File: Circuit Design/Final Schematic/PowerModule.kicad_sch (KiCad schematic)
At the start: 11 parts

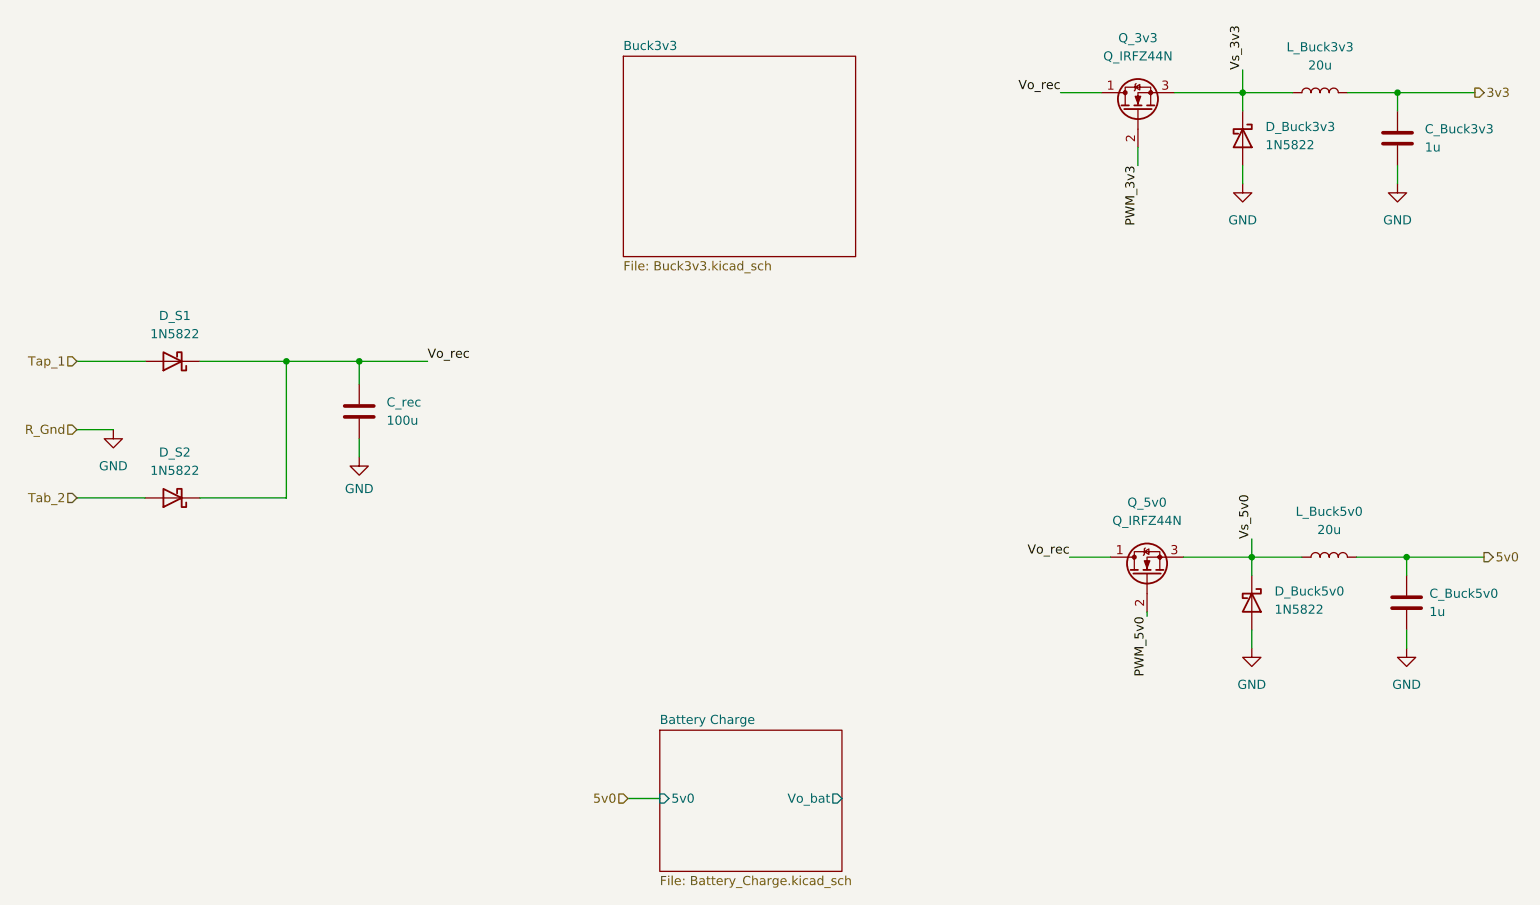
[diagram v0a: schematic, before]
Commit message: Power Module on schematic almost ready
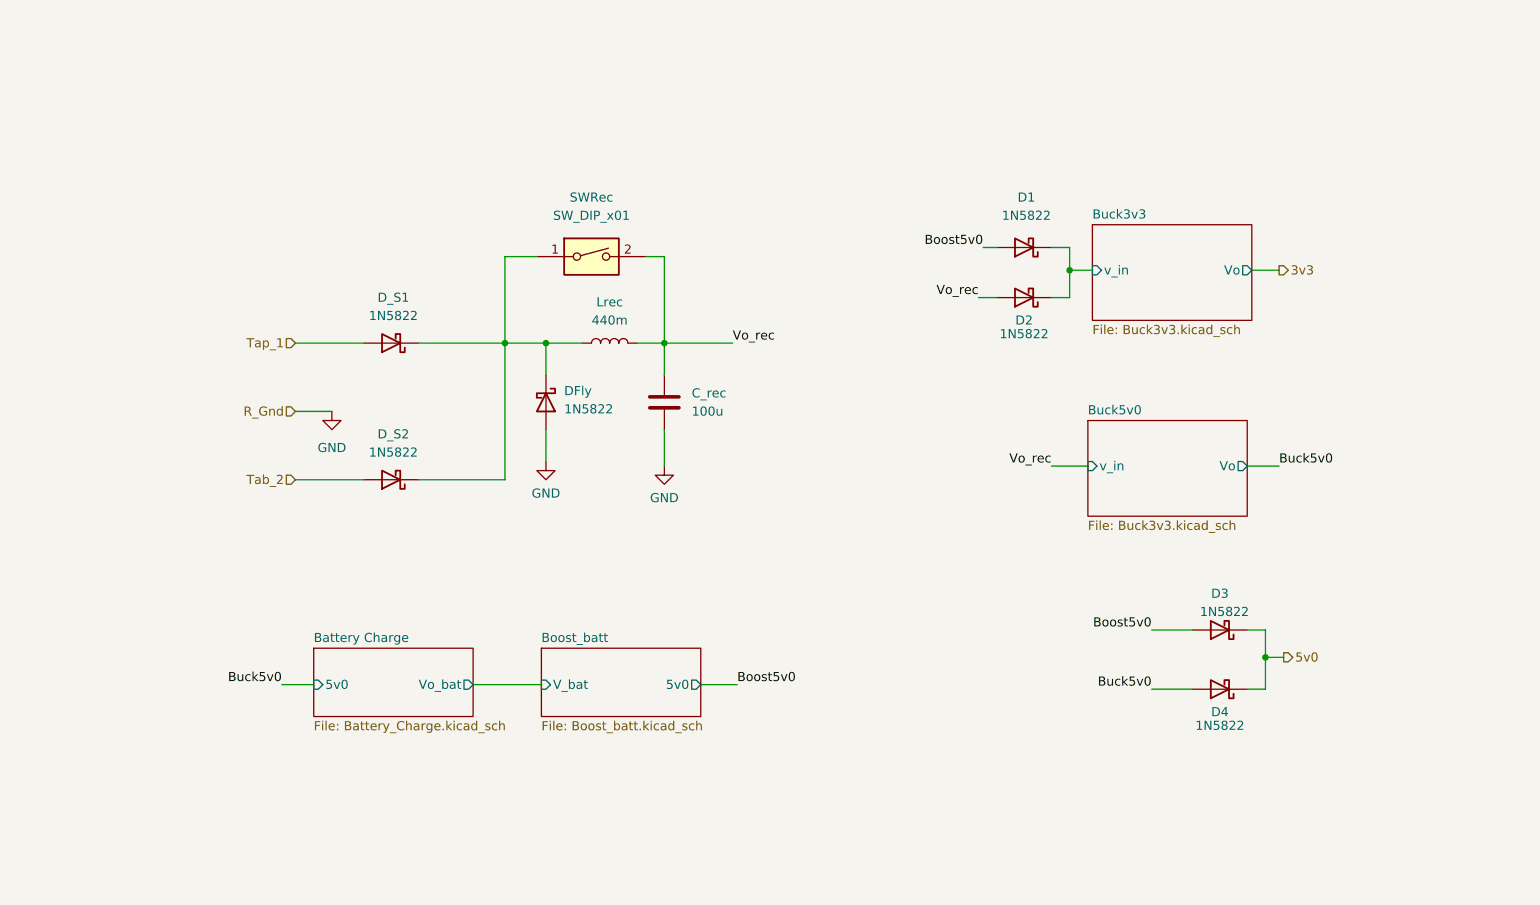
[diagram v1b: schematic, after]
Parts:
- removed C_Buck3v3, C_Buck5v0: 1u, Capacitor_SMD:CP_Elec_6.3x5.8, symbol Device:C
- removed D_Buck3v3, D_Buck5v0: 1N5822, Diode_THT:D_DO-201AD_P15.24mm_Horizontal, symbol Diode:1N5822
- removed L_Buck3v3, L_Buck5v0: 20u, Inductor_THT:L_Toroid_Vertical_L25.4mm_W14.7mm_P12.20mm_Vishay_TJ5_BigPads, symbol Device:L
- removed Q_3v3, Q_5v0: Q_IRFZ44N, Package_TO_SOT_THT:TO-220-3_Vertical, symbol Device:Q_NMOS_DGS
- added D1, D2, D3, D4, DFly: 1N5822, Diode_THT:D_DO-201AD_P15.24mm_Horizontal, symbol Diode:1N5822
- added Lrec: 440m, Inductor_THT:L_Toroid_Vertical_L25.4mm_W14.7mm_P12.20mm_Vishay_TJ5_BigPads, symbol Device:L
- added SWRec: SW_DIP_x01, symbol Switch:SW_DIP_x01
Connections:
- net 5v0: now also D3.1 (K), D4.1 (K)
- net GND: now also DFly.2 (A)
- net Vo_rec: now also D2.2 (A), Lrec.2, SWRec.2; no longer D_S1.1 (K), D_S2.1 (K)
- new net: DFly.1 (K), D_S1.1 (K), D_S2.1 (K), Lrec.1, SWRec.1
- new net Boost5v0: D1.2 (A), D3.2 (A)
- new net Buck3v3/v_in: D1.1 (K), D2.1 (K)
- new net Buck5v0: D4.2 (A)
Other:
- added sheet Boost_batt (Boost_batt.kicad_sch)
- added sheet Buck5v0 (Buck3v3.kicad_sch)
- sheet Buck3v3 ports: added Vo, v_in; removed none
- moved on the sheet: C_rec, D_S1, D_S2

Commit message: minor changes
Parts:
- SWRec: footprint (none) -> Connector_PinHeader_2.54mm:PinHeader_1x02_P2.54mm_Vertical_SMD_Pin1Left
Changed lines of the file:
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@@
     (property "Reference" "SWRec" (id 0) (at 116.205 57.15 0))
     (property "Value" "SW_DIP_x01" (id 1) (at 116.205 59.69 0))
-    (property "Footprint" "" (id 2) (at 116.205 65.405 0)
+    (property "Footprint" "Connector_PinHeader_2.54mm:PinHeader_1x02_P2.54mm_Vertical_SMD_Pin1Left" (id 2) (at 116.205 65.405 0)
       (effects (font (size 1.27 1.27)) hide)
     )

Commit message: Footprints
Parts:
- removed C_rec: 100u, Capacitor_SMD:C_0805_2012Metric_Pad1.18x1.45mm_HandSolder, symbol Device:C
- added Crec: 100u, Capacitor_THT:CP_Radial_D6.3mm_P2.50mm, symbol Device:C_Polarized
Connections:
- net GND: now also Crec.2
- net Vo_rec: now also Crec.1
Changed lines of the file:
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@@
+    (pin "2")
+  )
+  (symbol (lib_id "Device:C_Polarized") (at 126.365 85.725 0) (unit 1)
+    (in_bom yes) (on_board yes) (fields_autoplaced)
+    (property "Reference" "Crec" (id 0) (at 129.54 83.5659 0)
+      (effects (font (size 1.27 1.27)) (justify left))
+    )
+    (property "Value" "100u" (id 1) (at 129.54 86.1059 0)
+      (effects (font (size 1.27 1.27)) (justify left))
+    )
+    (property "Footprint" "Capacitor_THT:CP_Radial_D6.3mm_P2.50mm" (id 2) (at 127.3302 89.535 0)
+      (effects (font (size 1.27 1.27)) hide)
+    )
+    (property "Datasheet" "~" (id 3) (at 126.365 85.725 0)
+      (effects (font (size 1.27 1.27)) hide)
+    )
+    (pin "1")
     (pin "2")
   )
@@
       (effects (font (size 1.27 1.27)) hide)
     )
-    (pin "1")
-    (pin "2")
-  )
-  (symbol (lib_id "Device:C") (at 126.365 85.725 0) (unit 1)
-    (in_bom yes) (on_board yes) (fields_autoplaced)
-    (property "Reference" "C_rec" (id 0) (at 130.175 84.4549 0)
-      (effects (font (size 1.27 1.27)) (justify left))
-    )
-    (property "Value" "100u" (id 1) (at 130.175 86.9949 0)
-      (effects (font (size 1.27 1.27)) (justify left))
-    )
-    (property "Footprint" "Capacitor_SMD:C_0805_2012Metric_Pad1.18x1.45mm_HandSolder" (id 2) (at 127.3302 89.535 0)
-      (effects (font (size 1.27 1.27)) hide)
-    )
-    (property "Datasheet" "~" (id 3) (at 126.365 85.725 0)
-      (effects (font (size 1.27 1.27)) hide)
-    )

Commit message: Ferrite bead added
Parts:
- added FB?: FerriteBead, Resistor_SMD:R_1812_4532Metric_Pad1.30x3.40mm_HandSolder, symbol Device:FerriteBead
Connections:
- net GND: now also FB?.2
- new net R_Gnd: FB?.1
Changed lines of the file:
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@@
+    (stroke (width 0) (type default) (color 0 0 0 0))
+  )
+  (wire (pts (xy 74.93 86.995) (xy 76.835 86.995))
     (stroke (width 0) (type default) (color 0 0 0 0))
   )
@@
     (stroke (width 0) (type default) (color 0 0 0 0))
   )
-  (wire (pts (xy 74.93 86.995) (xy 80.01 86.995))
-    (stroke (width 0) (type default) (color 0 0 0 0))
-  )
   (wire (pts (xy 74.93 77.47) (xy 84.455 77.47))
     (stroke (width 0) (type default) (color 0 0 0 0))
@@
   )
   (wire (pts (xy 104.14 77.47) (xy 109.855 77.47))
+    (stroke (width 0) (type default) (color 0 0 0 0))
+  )
+  (wire (pts (xy 84.455 86.995) (xy 97.155 86.995))
     (stroke (width 0) (type default) (color 0 0 0 0))
   )
@@
     (pin "2")
   )
+  (symbol (lib_id "Device:FerriteBead") (at 80.645 86.995 90) (unit 1)
+    (in_bom yes) (on_board yes)
+    (property "Reference" "FB?" (id 0) (at 80.645 81.28 90))
+    (property "Value" "FerriteBead" (id 1) (at 80.645 83.185 90))
+    (property "Footprint" "Resistor_SMD:R_1812_4532Metric_Pad1.30x3.40mm_HandSolder" (id 2) (at 80.645 88.773 90)
+      (effects (font (size 1.27 1.27)) hide)
+    )
+    (property "Datasheet" "~" (id 3) (at 80.645 86.995 0)
+      (effects (font (size 1.27 1.27)) hide)
+    )
+    (pin "1")
+    (pin "2")
+  )
   (symbol (lib_id "power:GND") (at 126.365 94.615 0) (unit 1)
     (in_bom yes) (on_board yes) (fields_autoplaced)
@@
     (pin "2")
   )
-  (symbol (lib_id "power:GND") (at 80.01 86.995 0) (unit 1)
-    (in_bom yes) (on_board yes) (fields_autoplaced)
-    (property "Reference" "#PWR?" (id 0) (at 80.01 93.345 0)
-      (effects (font (size 1.27 1.27)) hide)
-    )
-    (property "Value" "GND" (id 1) (at 80.01 92.075 0))
-    (property "Footprint" "" (id 2) (at 80.01 86.995 0)
-      (effects (font (size 1.27 1.27)) hide)
-    )
-    (property "Datasheet" "" (id 3) (at 80.01 86.995 0)
-      (effects (font (size 1.27 1.27)) hide)
-    )
+  (symbol (lib_id "power:GND") (at 97.155 86.995 0) (unit 1)
+    (in_bom yes) (on_board yes) (fields_autoplaced)
+    (property "Reference" "#PWR?" (id 0) (at 97.155 93.345 0)
+      (effects (font (size 1.27 1.27)) hide)
+    )
+    (property "Value" "GND" (id 1) (at 97.155 92.075 0))
+    (property "Footprint" "" (id 2) (at 97.155 86.995 0)
+      (effects (font (size 1.27 1.27)) hide)
+    )
+    (property "Datasheet" "" (id 3) (at 97.155 86.995 0)
+      (effects (font (size 1.27 1.27)) hide)
+    )

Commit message: Footprints
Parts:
- gave numbers to parts that had none: 1
- renumbered Crec to Crec1, DFly to DFly1, Lrec to Lrec1, SWRec to SWRec1
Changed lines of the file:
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@@
   (symbol (lib_id "Diode:1N5822") (at 109.855 85.725 270) (unit 1)
     (in_bom yes) (on_board yes) (fields_autoplaced)
-    (property "Reference" "DFly" (id 0) (at 112.395 84.1374 90)
+    (property "Reference" "DFly1" (id 0) (at 112.395 84.1374 90)
       (effects (font (size 1.27 1.27)) (justify left))
     )
@@
   (symbol (lib_id "power:GND") (at 109.855 93.98 0) (unit 1)
     (in_bom yes) (on_board yes) (fields_autoplaced)
-    (property "Reference" "#PWR?" (id 0) (at 109.855 100.33 0)
+    (property "Reference" "#PWR0121" (id 0) (at 109.855 100.33 0)
       (effects (font (size 1.27 1.27)) hide)
     )
@@
   (symbol (lib_id "Switch:SW_DIP_x01") (at 116.205 65.405 0) (unit 1)
     (in_bom yes) (on_board yes) (fields_autoplaced)
-    (property "Reference" "SWRec" (id 0) (at 116.205 57.15 0))
+    (property "Reference" "SWRec1" (id 0) (at 116.205 57.15 0))
     (property "Value" "SW_DIP_x01" (id 1) (at 116.205 59.69 0))
     (property "Footprint" "Connector_PinHeader_2.54mm:PinHeader_1x02_P2.54mm_Vertical_SMD_Pin1Left" (id 2) (at 116.205 65.405 0)
@@
   (symbol (lib_id "Device:C_Polarized") (at 126.365 85.725 0) (unit 1)
     (in_bom yes) (on_board yes) (fields_autoplaced)
-    (property "Reference" "Crec" (id 0) (at 129.54 83.5659 0)
+    (property "Reference" "Crec1" (id 0) (at 129.54 83.5659 0)
       (effects (font (size 1.27 1.27)) (justify left))
     )
@@
   (symbol (lib_id "Device:FerriteBead") (at 80.645 86.995 90) (unit 1)
     (in_bom yes) (on_board yes)
-    (property "Reference" "FB?" (id 0) (at 80.645 81.28 90))
+    (property "Reference" "FB1" (id 0) (at 80.645 81.28 90))
     (property "Value" "FerriteBead" (id 1) (at 80.645 83.185 90))
     (property "Footprint" "Resistor_SMD:R_1812_4532Metric_Pad1.30x3.40mm_HandSolder" (id 2) (at 80.645 88.773 90)
@@
   (symbol (lib_id "power:GND") (at 126.365 94.615 0) (unit 1)
     (in_bom yes) (on_board yes) (fields_autoplaced)
-    (property "Reference" "#PWR?" (id 0) (at 126.365 100.965 0)
+    (property "Reference" "#PWR0122" (id 0) (at 126.365 100.965 0)
       (effects (font (size 1.27 1.27)) hide)
     )
@@
   (symbol (lib_id "Device:L") (at 118.745 77.47 90) (unit 1)
     (in_bom yes) (on_board yes) (fields_autoplaced)
-    (property "Reference" "Lrec" (id 0) (at 118.745 71.755 90))
+    (property "Reference" "Lrec1" (id 0) (at 118.745 71.755 90))
     (property "Value" "440m" (id 1) (at 118.745 74.295 90))
     (property "Footprint" "Inductor_THT:L_Toroid_Vertical_L25.4mm_W14.7mm_P12.20mm_Vishay_TJ5_BigPads" (id 2) (at 118.745 77.47 0)
@@
   (symbol (lib_id "power:GND") (at 97.155 86.995 0) (unit 1)
     (in_bom yes) (on_board yes) (fields_autoplaced)
-    (property "Reference" "#PWR?" (id 0) (at 97.155 93.345 0)
+    (property "Reference" "#PWR0120" (id 0) (at 97.155 93.345 0)
       (effects (font (size 1.27 1.27)) hide)
     )

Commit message: Mejor ruteo xd Felipe cambie las huellas
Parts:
- D3: footprint Diode_THT:D_DO-201AD_P15.24mm_Horizontal -> Diode_THT:D_DO-201AE_P5.08mm_Vertical_AnodeUp
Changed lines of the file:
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@@
     (property "Reference" "D3" (id 0) (at 203.835 112.395 0))
     (property "Value" "1N5822" (id 1) (at 204.47 114.935 0))
-    (property "Footprint" "Diode_THT:D_DO-201AD_P15.24mm_Horizontal" (id 2) (at 203.835 113.03 0)
+    (property "Footprint" "Diode_THT:D_DO-201AE_P5.08mm_Vertical_AnodeUp" (id 2) (at 203.835 113.03 0)
       (effects (font (size 1.27 1.27)) hide)
     )

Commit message: PCB distribution
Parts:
- D1, D2, D4, DFly1, D_S1, D_S2: footprint Diode_THT:D_DO-201AD_P15.24mm_Horizontal -> Diode_THT:D_DO-201AE_P5.08mm_Vertical_AnodeUp
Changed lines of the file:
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@@
     (property "Reference" "D_S2" (id 0) (at 88.5825 90.17 0))
     (property "Value" "1N5822" (id 1) (at 88.5825 92.71 0))
-    (property "Footprint" "Diode_THT:D_DO-201AD_P15.24mm_Horizontal" (id 2) (at 88.265 92.075 0)
+    (property "Footprint" "Diode_THT:D_DO-201AE_P5.08mm_Vertical_AnodeUp" (id 2) (at 88.265 92.075 0)
       (effects (font (size 1.27 1.27)) hide)
     )
@@
       (effects (font (size 1.27 1.27)) (justify left))
     )
-    (property "Footprint" "Diode_THT:D_DO-201AD_P15.24mm_Horizontal" (id 2) (at 105.41 85.725 0)
+    (property "Footprint" "Diode_THT:D_DO-201AE_P5.08mm_Vertical_AnodeUp" (id 2) (at 105.41 85.725 0)
       (effects (font (size 1.27 1.27)) hide)
     )
@@
     (property "Reference" "D1" (id 0) (at 176.8475 57.15 0))
     (property "Value" "1N5822" (id 1) (at 176.8475 59.69 0))
-    (property "Footprint" "Diode_THT:D_DO-201AD_P15.24mm_Horizontal" (id 2) (at 176.53 59.69 0)
+    (property "Footprint" "Diode_THT:D_DO-201AE_P5.08mm_Vertical_AnodeUp" (id 2) (at 176.53 59.69 0)
       (effects (font (size 1.27 1.27)) hide)
     )
@@
     (property "Reference" "D4" (id 0) (at 203.835 128.905 0))
     (property "Value" "1N5822" (id 1) (at 203.835 130.81 0))
-    (property "Footprint" "Diode_THT:D_DO-201AD_P15.24mm_Horizontal" (id 2) (at 203.835 121.285 0)
+    (property "Footprint" "Diode_THT:D_DO-201AE_P5.08mm_Vertical_AnodeUp" (id 2) (at 203.835 121.285 0)
       (effects (font (size 1.27 1.27)) hide)
     )
@@
     (property "Reference" "D_S1" (id 0) (at 88.5825 71.12 0))
     (property "Value" "1N5822" (id 1) (at 88.5825 73.66 0))
-    (property "Footprint" "Diode_THT:D_DO-201AD_P15.24mm_Horizontal" (id 2) (at 88.265 73.025 0)
+    (property "Footprint" "Diode_THT:D_DO-201AE_P5.08mm_Vertical_AnodeUp" (id 2) (at 88.265 73.025 0)
       (effects (font (size 1.27 1.27)) hide)
     )
@@
     (property "Reference" "D2" (id 0) (at 176.53 74.295 0))
     (property "Value" "1N5822" (id 1) (at 176.53 76.2 0))
-    (property "Footprint" "Diode_THT:D_DO-201AD_P15.24mm_Horizontal" (id 2) (at 176.53 66.675 0)
+    (property "Footprint" "Diode_THT:D_DO-201AE_P5.08mm_Vertical_AnodeUp" (id 2) (at 176.53 66.675 0)
       (effects (font (size 1.27 1.27)) hide)
     )

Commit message: More free space schematic
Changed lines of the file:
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@@
   (symbol (lib_id "Diode:1N5822") (at 88.265 96.52 180) (unit 1)
     (in_bom yes) (on_board yes) (fields_autoplaced)
-    (property "Reference" "D_S2" (id 0) (at 88.5825 90.17 0))
+    (property "Reference" "D_S2" (id 0) (at 88.5825 90.17 0)
+      (effects (font (size 1.27 1.27)) hide)
+    )
     (property "Value" "1N5822" (id 1) (at 88.5825 92.71 0))
     (property "Footprint" "Diode_THT:D_DO-201AE_P5.08mm_Vertical_AnodeUp" (id 2) (at 88.265 92.075 0)
@@
     (in_bom yes) (on_board yes) (fields_autoplaced)
     (property "Reference" "DFly1" (id 0) (at 112.395 84.1374 90)
-      (effects (font (size 1.27 1.27)) (justify left))
+      (effects (font (size 1.27 1.27)) (justify left) hide)
     )
     (property "Value" "1N5822" (id 1) (at 112.395 86.6774 90)
@@
     (in_bom yes) (on_board yes) (fields_autoplaced)
     (property "Reference" "Crec1" (id 0) (at 129.54 83.5659 0)
-      (effects (font (size 1.27 1.27)) (justify left))
+      (effects (font (size 1.27 1.27)) (justify left) hide)
     )
     (property "Value" "100u" (id 1) (at 129.54 86.1059 0)
